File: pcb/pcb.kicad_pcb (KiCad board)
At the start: 2 copper layers, 110 x 124 mm, 64 parts, among them J1 AMT0440007DB0000G, J10 Conn_02x10_Odd_Even, J11 Conn_01x03, J12 Conn_01x02, J14 Conn_01x04, J15 Conn_01x10, J16 Conn_01x10, J2 AMT0440007DB0000G, J3 AMT0440007DB0000G, J4 AMT0440007DB0000G, J5 Conn_01x03, J6 Conn_01x03, J7 Conn_01x03, J8 Conn_01x03, J9 Conn_01x03, Q1 IRF9Z34NPBF, Q2 IRF9Z34NPBF, Q3 IRF9Z34NPBF, Q4 IRF9Z34NPBF, Q5 IRF9Z34NPBF, U1 ACS711ELCTR-12AB-T, U2 ACS711ELCTR-12AB-T, U3 ACS711ELCTR-12AB-T, U4 ACS711ELCTR-12AB-T, U5 ACS711ELCTR-12AB-T, U6 TXS0102DCUR, U7 TXS0102DCUR, U8 TXS0102DCUR, U9 NCP718BSNADJT1G

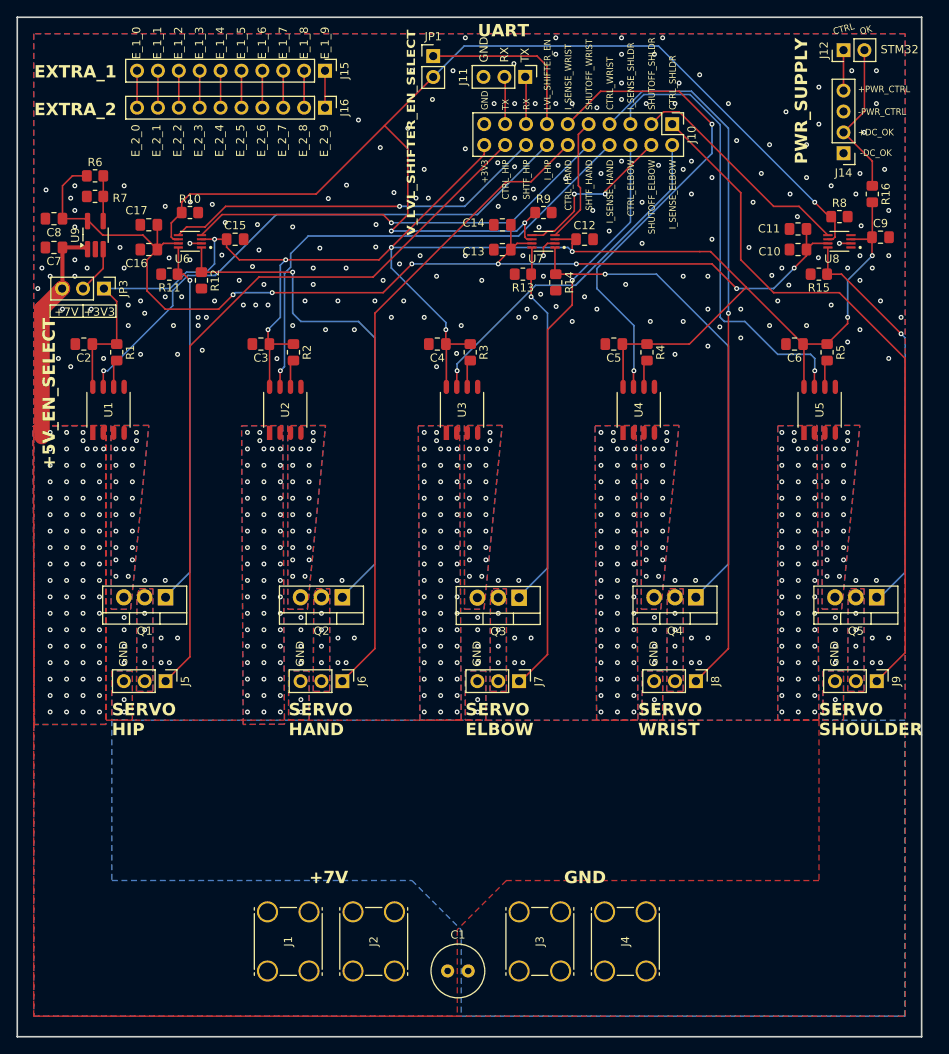
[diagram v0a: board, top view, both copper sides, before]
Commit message: Add silkscreen info about PCB and tidy silkscreen
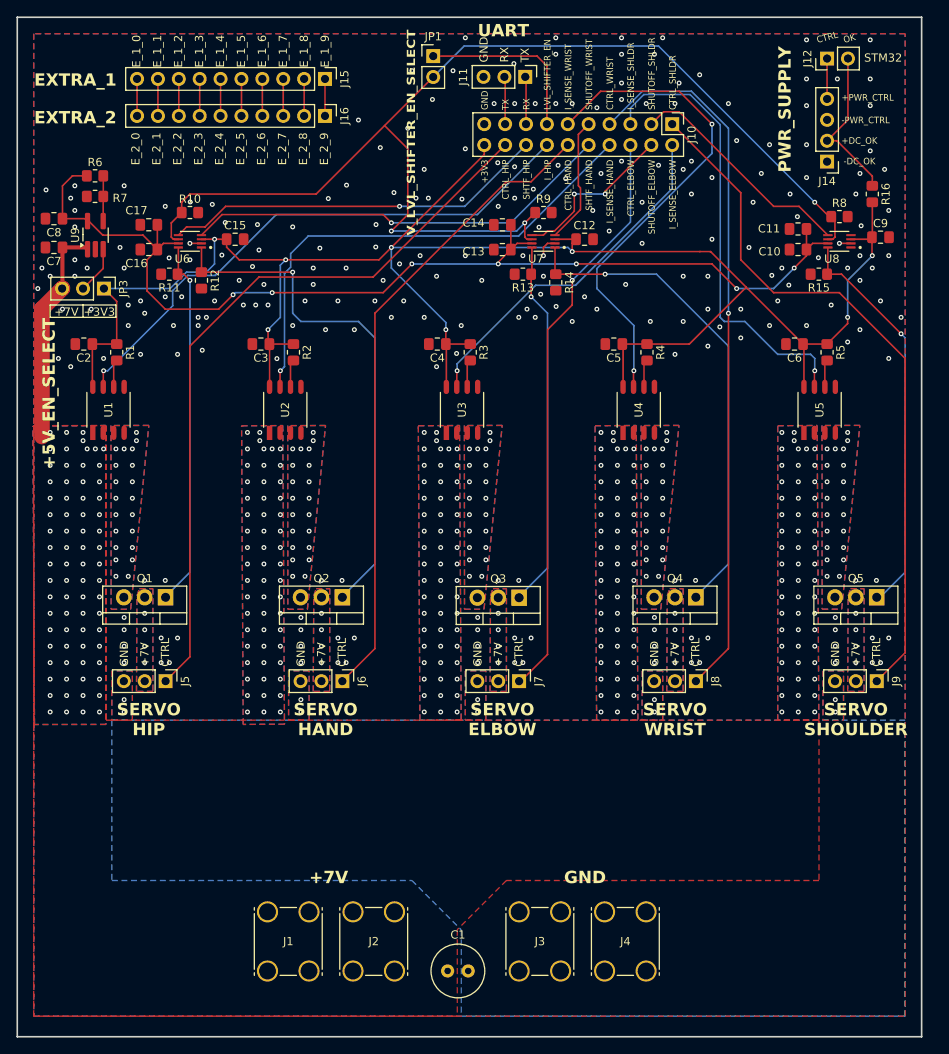
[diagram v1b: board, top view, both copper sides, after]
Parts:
- moved J14 2.25 mm to (190.5, 43.1)
- moved J12 2.25 mm to (190.5, 30.5)
- moved J15 1.00 mm to (129.4, 33.0)
- moved J16 1.00 mm to (129.4, 37.5)
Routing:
- net +DC_OK: track 19.0 -> 19.5 mm
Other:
- board text added: "Vision Arm v1 2026-10-10 Schematic and Layout by Josh Martin"

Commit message: Add PCB mounting holes
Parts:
- added REF**: MountingHole_4.3mm_M4, MountingHole:MountingHole_4.3mm_M4, F.Cu at (197.2, 144.8)
- added REF**: MountingHole_4.3mm_M4, MountingHole:MountingHole_4.3mm_M4, F.Cu at (96.8, 144.8)
- added REF**: MountingHole_4.3mm_M4, MountingHole:MountingHole_4.3mm_M4, F.Cu at (96.8, 30.2)
- added REF**: MountingHole_4.3mm_M4, MountingHole:MountingHole_4.3mm_M4, F.Cu at (197.2, 30.2)
- moved J15 2.73 mm to (126.7, 33.0)
- moved J16 2.73 mm to (126.7, 37.5)
- moved J14 1.90 mm to (192.2, 43.8)
- moved J12 0.75 mm to (189.8, 30.5), turned to -90 degrees
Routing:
- net +PWR_CTRL: track 4.92 -> 6.73 mm
- net GNDREF: vias 253 -> 247
- net (no net): vias 0 -> 2

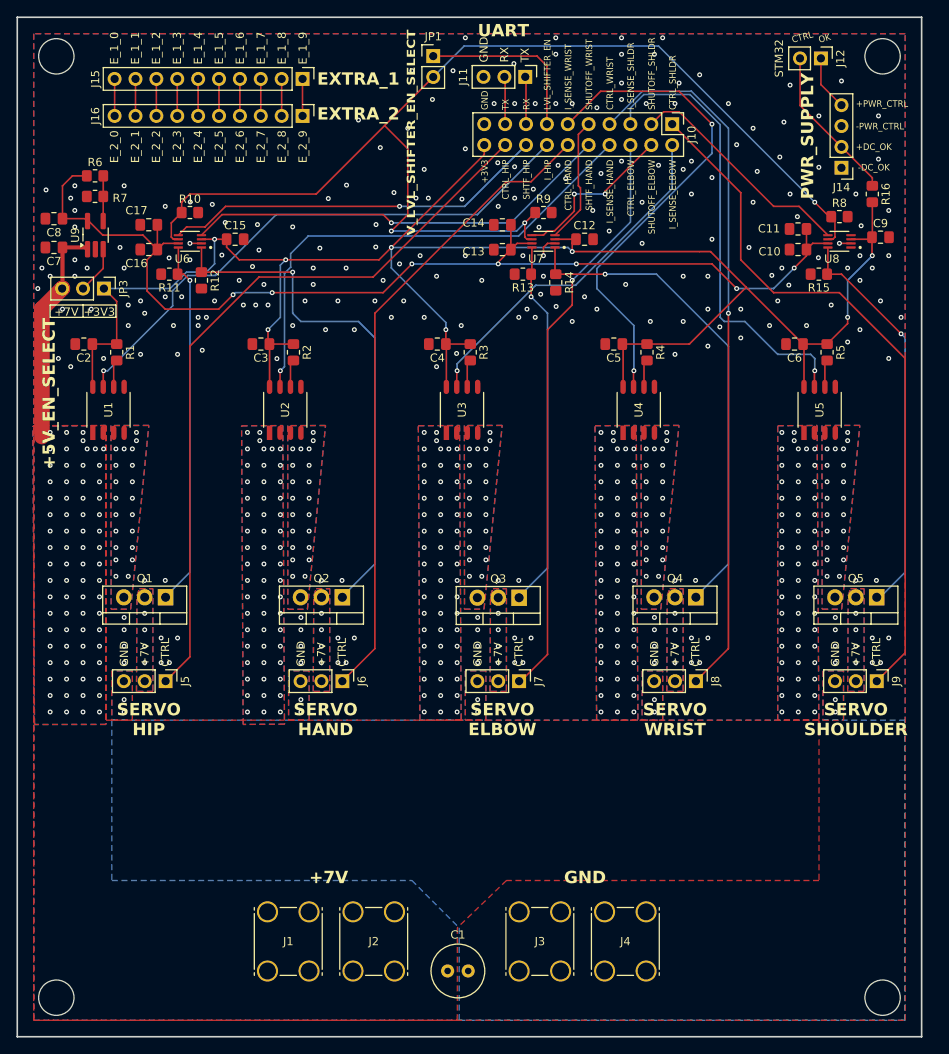
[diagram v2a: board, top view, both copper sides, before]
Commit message: Fix vias with no net and hole in ground plane
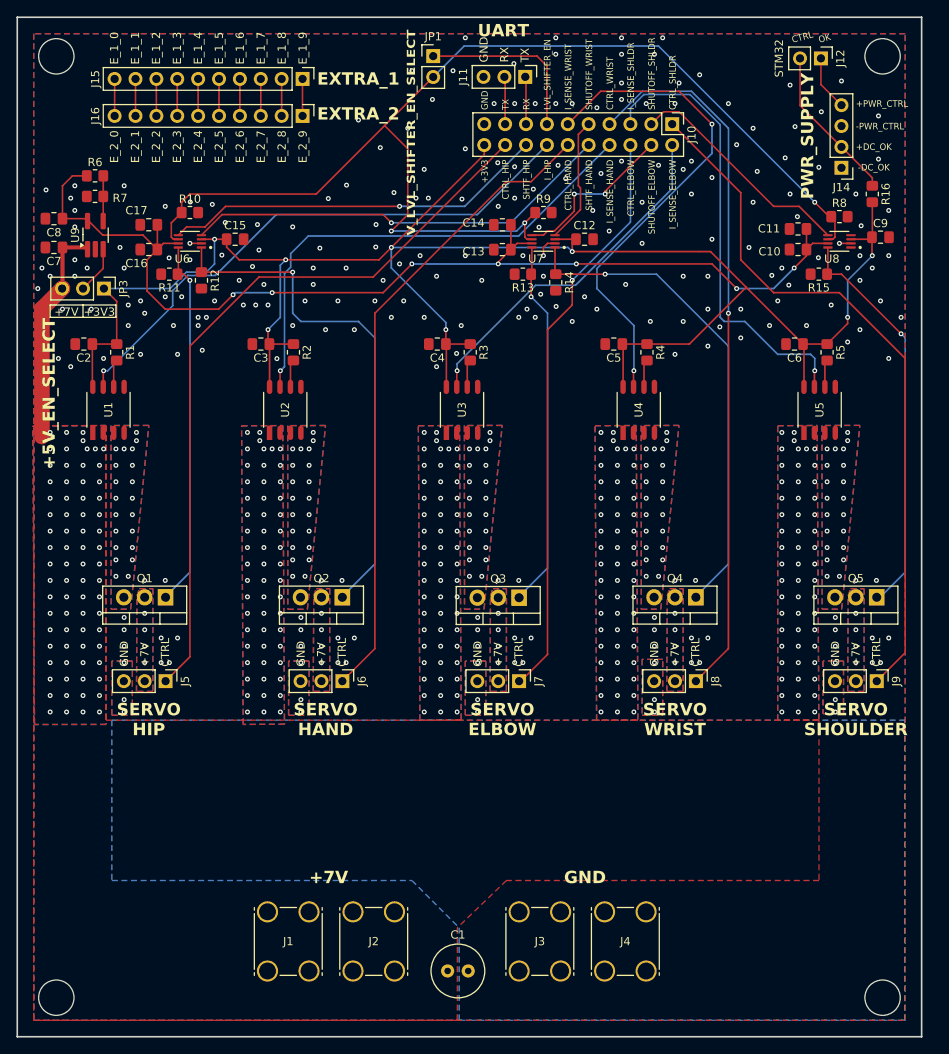
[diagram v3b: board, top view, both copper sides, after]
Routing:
- net GNDREF: vias 247 -> 249
- net (no net): vias 2 -> 0
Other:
- board text added: "Vision Arm v1 2026-10-11 Schematic and Layout by Josh Martin"
- board text removed: "Vision Arm v1 2026-10-10 Schematic and Layout by Josh Martin"
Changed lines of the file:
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@@
 		(capping no)
 		(filling no)
-		(zone_defaults)
 		(pcbplotparams
 			(layerselection 0x00000000_00000000_55555555_5755f5ff)
@@
 		)
 	)
-	(gr_text "Vision Arm v1\n2026-10-10\n\nSchematic and Layout by Josh Martin"
+	(gr_text "Vision Arm v1\n2026-10-11\n\nSchematic and Layout by Josh Martin"
 		(at 191.5 147.5 0)
 		(layer "B.SilkS")
@@
 		)
 	)
-	(via
-		(at 185.25 38.25)
-		(size 0.6)
-		(drill 0.3)
-		(layers "F.Cu" "B.Cu")
-		(net "")
-	)
-	(via
-		(at 184.75 42.5)
-		(size 0.6)
-		(drill 0.3)
-		(layers "F.Cu" "B.Cu")
-		(net "")
-	)
 	(segment
 		(start 97.46 58.5)
@@
 	)
 	(via
+		(at 186.6 38.8)
+		(size 0.6)
+		(drill 0.3)
+		(layers "F.Cu" "B.Cu")
+		(free yes)
+		(net "GNDREF")
+	)
+	(via
 		(at 176 65.5)
 		(size 0.6)
@@
 	)
 	(via
-		(at 189.5 37.5)
+		(at 189.8 37)
 		(size 0.6)
 		(drill 0.3)
@@
 	)
 	(via
+		(at 185.4 42.6)
+		(size 0.6)
+		(drill 0.3)
+		(layers "F.Cu" "B.Cu")
+		(net "GNDREF")
+	)
+	(via
 		(at 129 94)
 		(size 0.6)
@@
 		(polygon
 			(pts
-				(xy 192.5 105) (xy 190 105) (xy 190 111) (xy 192.5 111)
+				(xy 192.5 103.8) (xy 190 103.8) (xy 190 110.2) (xy 192.5 110.2)
 			)
 		)
@@
 		(polygon
 			(pts
-				(xy 106 105) (xy 103.5 105) (xy 103.5 111) (xy 106 111)
+				(xy 106 103.8) (xy 103.5 103.8) (xy 103.5 110.4) (xy 106 110.4)
 			)
 		)
@@
 		(polygon
 			(pts
-				(xy 127.5 105) (xy 125 105) (xy 125 111) (xy 127.5 111)
+				(xy 127.5 103.8) (xy 125 103.8) (xy 125 110.4) (xy 127.5 110.4)
 			)
 		)
@@
 		(polygon
 			(pts
-				(xy 170.5 105) (xy 168 105) (xy 168 111) (xy 170.5 111)
+				(xy 170.5 103.6) (xy 168 103.6) (xy 168 110.4) (xy 170.5 110.4)
 			)
 		)
@@
 		(polygon
 			(pts
-				(xy 149 105) (xy 146.5 105) (xy 146.5 111) (xy 149 111)
+				(xy 149 103.8) (xy 146.5 103.8) (xy 146.5 110.4) (xy 149 110.4)
 			)
 		)
